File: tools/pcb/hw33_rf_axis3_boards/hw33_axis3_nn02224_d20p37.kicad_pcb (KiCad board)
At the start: 2 copper layers, 20.4 x 20.4 mm, 6 parts, among them J1 U.FL-R-SMT-1

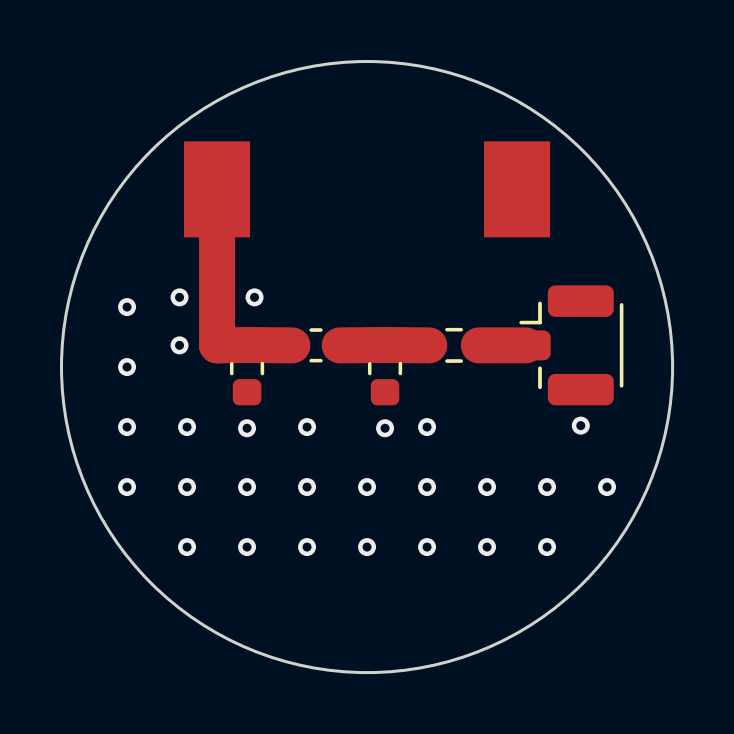
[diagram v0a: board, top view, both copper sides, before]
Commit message: HW.33 · фікси за адверсаром 037b77bc3: стартова мережа — Т із CR80, «П-ланка» знята як хибна топологія, корпус бустера — у перевірці контуру
Адверсар знайшов, що моя ж дописка «eval-ланка — Г, не П» узагальнила одну
плату з трьох: AN_NN02-224_ISM має в нашій смузі Г на 131 × 60 (863–870), Т на
131 × 60 (863–928) і Т на CR80 86 × 54 (863–870; 30 · 13 шунт · 3 nH) — а CR80
найближча до нашої землі. Звірено рендером сторінки 19. Стартова точка тюнінгу
тепер — Т на сайтах B · C · D (аркуш стенда §5, README, шапка генератора).

Звідси клас ширший за дописку: «П-ланка» стояла в 14 місцях канону, трекера й
аркушів, а 02_01 §5.3 називав «посадкові місця під П-ланку» вимогою «обох
app-note дослівно» — app-note каже «matching network», топології не називаючи,
а в прочитаних мережах NN02-224 П немає жодного разу; П-посадка Т не вміщає.
Назва — за функцією («узгоджувальна ланка») скрізь; у домі вимоги (02_01 §5.3)
і в 👤-нозі розкладки HW.9 — заборона «не під П-ланку» з підставою.

Генератор: корпус бустера — частина розміщення й перевірки контуру (корпус
NN02-201 7.0 × 3.0 ширший за пади й стояв 0.05 мм від краю — UM_NN02-201 §2.1);
провенанс NN02-201 — sha256 і власний посібник (монтажний пад «must NOT be
grounded», стор. 11); вертикальна ланка зсунута на 1 мм до центру, щоб U.FL
лишився в контурі; паркан via може заходити в кортьярди деталей ланки (не в
пади); плата, що не пройшла DRC, видаляється разом із проєктом; площа
clearance-сегмента друкується — 30–33 % диска для NN02-224, 18–20 % для NN02-201
(«найвужча» ≠ «мала»: тепер це сказано числом у README, аркуші й нозі).

Тексти, що казали сильніше за плату, приведено до виміру: «via біля кожного
GND-паду» — неправда для U.FL на трьох платах (другий пад — 3–4 мм, λ_g/50);
«≈ λ/22» — число доби Ø15.57, на наших дисках λ/17–18 (і в домі числа 02_01 §5.3
— дописка); набір для тюнінгу — з деталей, які називає сам виробник (LQW18AN 0603,
LQW15AN і GJM1555 0402), а не з памʼяті.

Ще два члени класу: калькулятор площі рахує кортьяр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
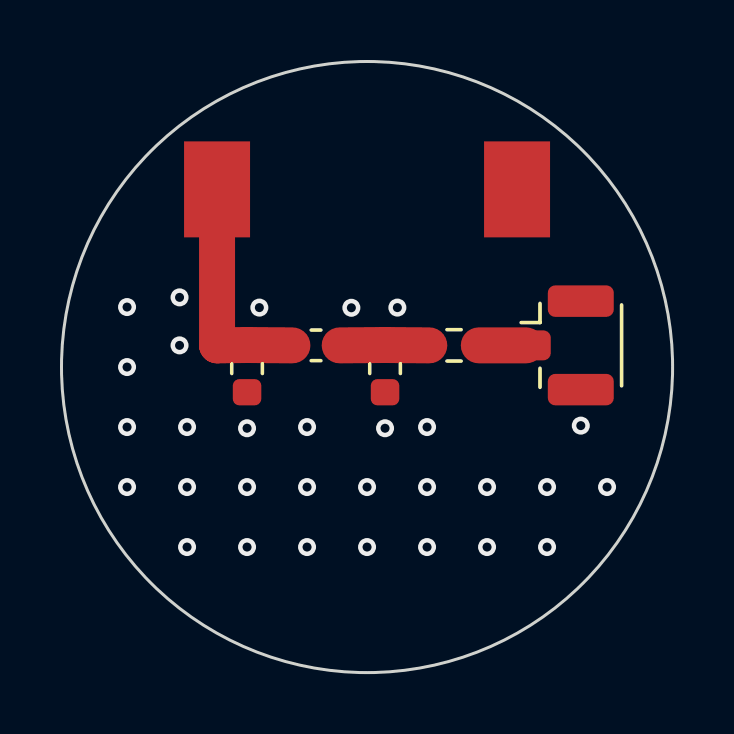
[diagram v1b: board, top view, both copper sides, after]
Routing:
- net GND: vias 28 -> 30
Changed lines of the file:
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@@
 		)
 		(fp_line
-			(start -6.1 -1.6)
-			(end 6.1 -1.6)
+			(start -6 -1.5)
+			(end 6 -1.5)
 			(stroke
 				(width 0.1)
@@
 		)
 		(fp_line
-			(start -6.1 1.6)
-			(end -6.1 -1.6)
+			(start -6 1.5)
+			(end -6 -1.5)
 			(stroke
 				(width 0.1)
@@
 		)
 		(fp_line
-			(start 6.1 -1.6)
-			(end 6.1 1.6)
+			(start 6 -1.5)
+			(end 6 1.5)
 			(stroke
 				(width 0.1)
@@
 		)
 		(fp_line
-			(start 6.1 1.6)
-			(end -6.1 1.6)
+			(start 6 1.5)
+			(end -6 1.5)
 			(stroke
 				(width 0.1)
@@
 	)
 	(via
+		(at -4 6)
+		(size 0.6)
+		(drill 0.3)
+		(layers "F.Cu" "B.Cu")
+		(net "GND")
+	)
+	(via
+		(at -4 2.039918)
+		(size 0.6)
+		(drill 0.3)
+		(layers "F.Cu" "B.Cu")
+		(net "GND")
+	)
+	(via
+		(at 0.599999 2.039918)
+		(size 0.6)
+		(drill 0.3)
+		(layers "F.Cu" "B.Cu")
+		(net "GND")
+	)
+	(via
+		(at 2 2)
+		(size 0.6)
+		(drill 0.3)
+		(layers "F.Cu" "B.Cu")
+		(net "GND")
+	)
+	(via
+		(at -8 0)
+		(size 0.6)
+		(drill 0.3)
+		(layers "F.Cu" "B.Cu")
+		(net "GND")
+	)
+	(via
+		(at -8 -2)
+		(size 0.6)
+		(drill 0.3)
+		(layers "F.Cu" "B.Cu")
+		(net "GND")
+	)
+	(via
+		(at -6.25 -2.322581)
+		(size 0.6)
+		(drill 0.3)
+		(layers "F.Cu" "B.Cu")
+		(net "GND")
+	)
+	(via
+		(at -8 2)
+		(size 0.6)
+		(drill 0.3)
+		(layers "F.Cu" "B.Cu")
+		(net "GND")
+	)
+	(via
+		(at -6 2)
+		(size 0.6)
+		(drill 0.3)
+		(layers "F.Cu" "B.Cu")
+		(net "GND")
+	)
+	(via
 		(at -2 4)
 		(size 0.6)
@@
 	)
 	(via
-		(at -4 2.039918)
-		(size 0.6)
-		(drill 0.3)
-		(layers "F.Cu" "B.Cu")
-		(net "GND")
-	)
-	(via
-		(at 0.599999 2.039918)
+		(at 2 4)
+		(size 0.6)
+		(drill 0.3)
+		(layers "F.Cu" "B.Cu")
+		(net "GND")
+	)
+	(via
+		(at -0.522844 -1.975844)
+		(size 0.6)
+		(drill 0.3)
+		(layers "F.Cu" "B.Cu")
+		(net "GND")
+	)
+	(via
+		(at 6 6)
+		(size 0.6)
+		(drill 0.3)
+		(layers "F.Cu" "B.Cu")
+		(net "GND")
+	)
+	(via
+		(at 6 4)
+		(size 0.6)
+		(drill 0.3)
+		(layers "F.Cu" "B.Cu")
+		(net "GND")
+	)
+	(via
+		(at -4 4)
+		(size 0.6)
+		(drill 0.3)
+		(layers "F.Cu" "B.Cu")
+		(net "GND")
+	)
+	(via
+		(at -6.25 -0.72258)
+		(size 0.6)
+		(drill 0.3)
+		(layers "F.Cu" "B.Cu")
+		(net "GND")
+	)
+	(via
+		(at 7.125 1.952419)
+		(size 0.6)
+		(drill 0.3)
+		(layers "F.Cu" "B.Cu")
+		(net "GND")
+	)
+	(via
+		(at 4 6)
+		(size 0.6)
+		(drill 0.3)
+		(layers "F.Cu" "B.Cu")
+		(net "GND")
+	)
+	(via
+		(at 8 4)
+		(size 0.6)
+		(drill 0.3)
+		(layers "F.Cu" "B.Cu")
+		(net "GND")
+	)
+	(via
+		(at -6 4)
+		(size 0.6)
+		(drill 0.3)
+		(layers "F.Cu" "B.Cu")
+		(net "GND")
+	)
+	(via
+		(at -8 4)
+		(size 0.6)
+		(drill 0.3)
+		(layers "F.Cu" "B.Cu")
+		(net "GND")
+	)
+	(via
+		(at -2 2)
+		(size 0.6)
+		(drill 0.3)
+		(layers "F.Cu" "B.Cu")
+		(net "GND")
+	)
+	(via
+		(at -3.589682 -1.981733)
+		(size 0.6)
+		(drill 0.3)
+		(layers "F.Cu" "B.Cu")
+		(net "GND")
+	)
+	(via
+		(at -6 6)
+		(size 0.6)
+		(drill 0.3)
+		(layers "F.Cu" "B.Cu")
+		(net "GND")
+	)
+	(via
+		(at 0 4)
+		(size 0.6)
+		(drill 0.3)
+		(layers "F.Cu" "B.Cu")
+		(net "GND")
+	)
+	(via
+		(at 4 4)
 		(size 0.6)
 		(drill 0.3)
@@
 	)
 	(via
-		(at -8 4)
-		(size 0.6)
-		(drill 0.3)
-		(layers "F.Cu" "B.Cu")
-		(net "GND")
-	)
-	(via
-		(at -8 2)
-		(size 0.6)
-		(drill 0.3)
-		(layers "F.Cu" "B.Cu")
-		(net "GND")
-	)
-	(via
-		(at -8 -2)
-		(size 0.6)
-		(drill 0.3)
-		(layers "F.Cu" "B.Cu")
-		(net "GND")
-	)
-	(via
-		(at -6 2)
-		(size 0.6)
-		(drill 0.3)
-		(layers "F.Cu" "B.Cu")
-		(net "GND")
-	)
-	(via
-		(at -6 6)
-		(size 0.6)
-		(drill 0.3)
-		(layers "F.Cu" "B.Cu")
-		(net "GND")
-	)
-	(via
-		(at 0 4)
-		(size 0.6)
-		(drill 0.3)
-		(layers "F.Cu" "B.Cu")
-		(net "GND")
-	)
-	(via
-		(at 4 4)
-		(size 0.6)
-		(drill 0.3)
-		(layers "F.Cu" "B.Cu")
-		(net "GND")
-	)
-	(via
-		(at -3.75 -2.322581)
-		(size 0.6)
-		(drill 0.3)
-		(layers "F.Cu" "B.Cu")
-		(net "GND")
-	)
-	(via
-		(at 8 4)
-		(size 0.6)
-		(drill 0.3)
-		(layers "F.Cu" "B.Cu")
-		(net "GND")
-	)
-	(via
-		(at -2 2)
-		(size 0.6)
-		(drill 0.3)
-		(layers "F.Cu" "B.Cu")
-		(net "GND")
-	)
-	(via
-		(at -8 0)
-		(size 0.6)
-		(drill 0.3)
-		(layers "F.Cu" "B.Cu")
-		(net "GND")
-	)
-	(via
-		(at 7.125 1.952419)
-		(size 0.6)
-		(drill 0.3)
-		(layers "F.Cu" "B.Cu")
-		(net "GND")
-	)
-	(via
-		(at 6 6)
-		(size 0.6)
-		(drill 0.3)
-		(layers "F.Cu" "B.Cu")
-		(net "GND")
-	)
-	(via
-		(at -4 4)
-		(size 0.6)
-		(drill 0.3)
-		(layers "F.Cu" "B.Cu")
-		(net "GND")
-	)
-	(via
-		(at -6 4)
+		(at 0 6)
+		(size 0.6)
+		(drill 0.3)
+		(layers "F.Cu" "B.Cu")
+		(net "GND")
+	)
+	(via
+		(at 1.010578 -1.981647)
 		(size 0.6)
 		(drill 0.3)
@@
 		(size 0.6)
 		(drill 0.3)
-		(layers "F.Cu" "B.Cu")
-		(net "GND")
-	)
-	(via
-		(at -6.25 -0.72258)
-		(size 0.6)
-		(drill 0.3)
-		(layers "F.Cu" "B.Cu")
-		(net "GND")
-	)
-	(via
-		(at -4 6)
-		(size 0.6)
-		(drill 0.3)
-		(layers "F.Cu" "B.Cu")
-		(net "GND")
-	)
-	(via
-		(at 2 2)
-		(size 0.6)
-		(drill 0.3)
-		(layers "F.Cu" "B.Cu")
-		(net "GND")
-	)
-	(via
-		(at 6 4)
-		(size 0.6)
-		(drill 0.3)
-		(layers "F.Cu" "B.Cu")
-		(net "GND")
-	)
-	(via
-		(at 4 6)
-		(size 0.6)
-		(drill 0.3)
-		(layers "F.Cu" "B.Cu")
-		(net "GND")
-	)
-	(via
-		(at 2 4)
-		(size 0.6)
-		(drill 0.3)
-		(layers "F.Cu" "B.Cu")
-		(net "GND")
-	)
-	(via
-		(at -6.25 -2.322581)
-		(size 0.6)
-		(drill 0.3)
-		(layers "F.Cu" "B.Cu")
-		(net "GND")
-	)
-	(via
-		(at 0 6)
-		(size 0.6)
-		(drill 0.3)
